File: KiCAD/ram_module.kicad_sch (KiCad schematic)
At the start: 2 parts, among them U30 CY7C199, U31 CY7C199

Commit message: finished schematics and footprint assignments; need to figure out +5v connection issue
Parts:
- U30, U31: footprint (none) -> Package_DIP:DIP-28_W7.62mm
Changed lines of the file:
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@@
 			)
 		)
-		(property "Footprint" ""
+		(property "Footprint" "Package_DIP:DIP-28_W7.62mm"
 			(at 213.36 66.04 0)
 			(effects
@@
 			)
 		)
-		(property "Footprint" ""
+		(property "Footprint" "Package_DIP:DIP-28_W7.62mm"
 			(at 153.67 66.04 0)
 			(effects

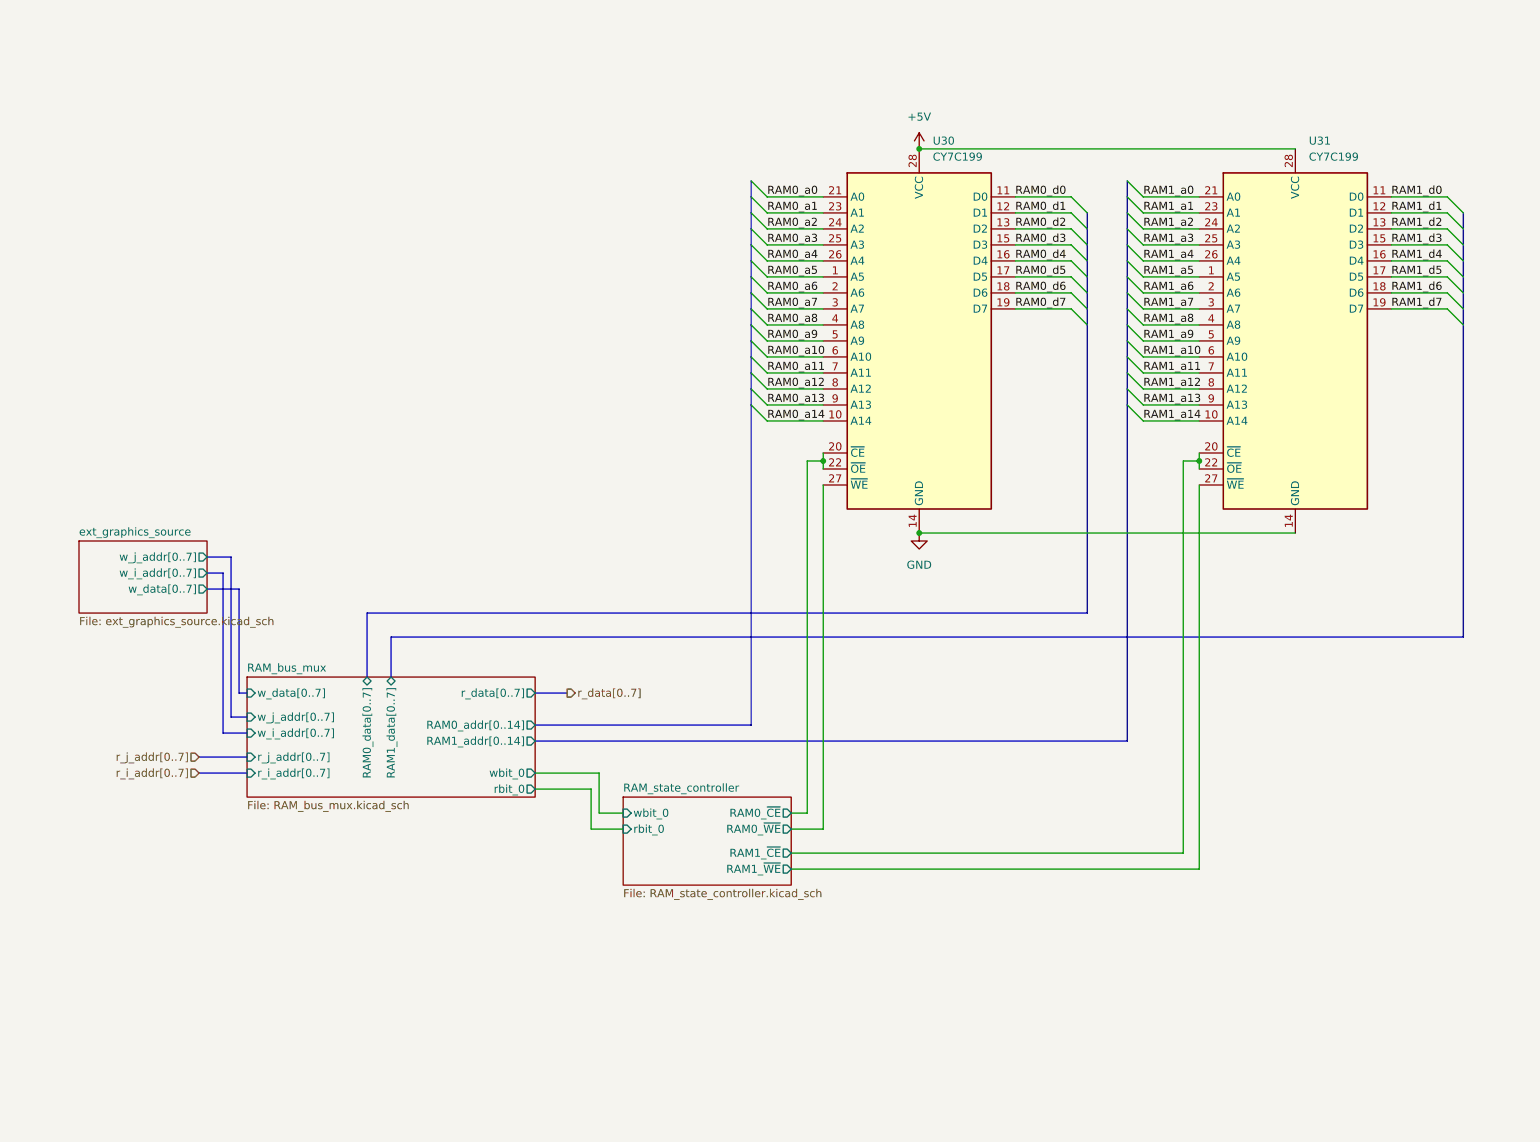
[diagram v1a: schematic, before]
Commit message: modified debug connector; changed board type in pcb editor
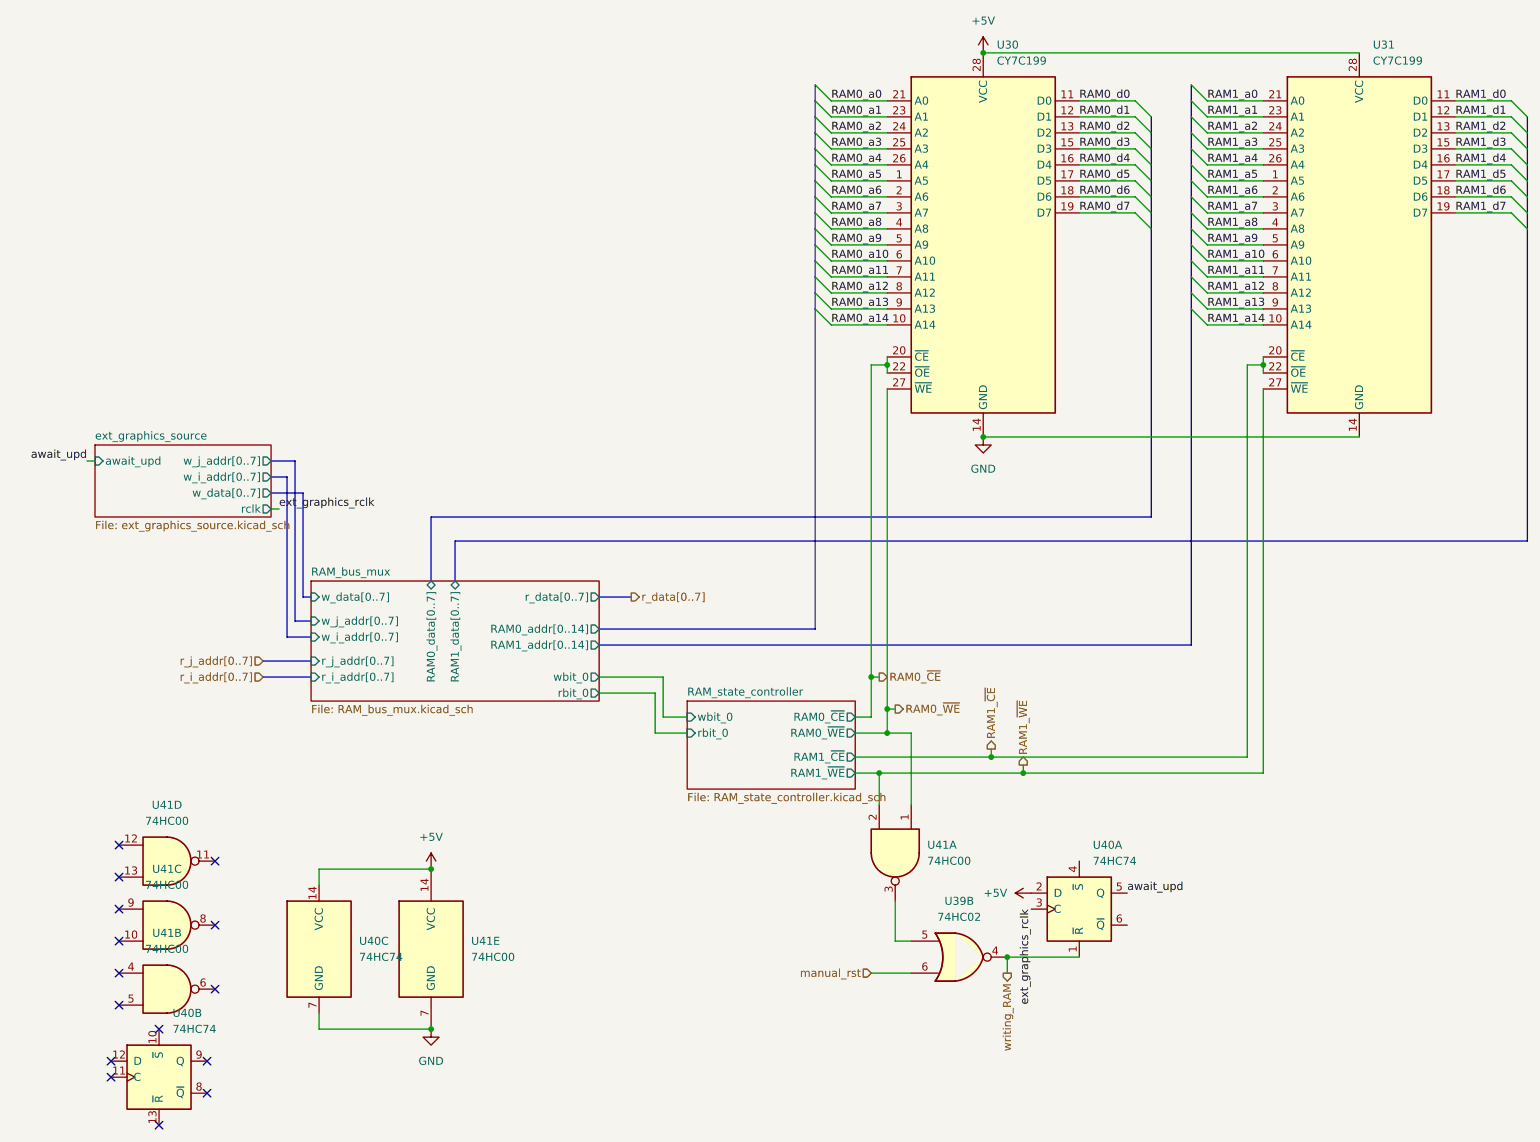
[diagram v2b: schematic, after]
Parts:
- added U39: 74HC02, Package_DIP:DIP-14_W7.62mm, symbol 74xx:74HC02
- added U40: 74HC74, Package_DIP:DIP-14_W7.62mm, symbol 74xx:74HC74
- added U41: 74HC00, Package_DIP:DIP-14_W7.62mm, symbol 74xx:74HC00
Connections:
- net +5V: now also U40.14 (VCC), U40.2 (D), U41.14 (VCC)
- net GND: now also U40.7 (GND), U41.7 (GND)
- net RAM_state_controller/RAM0_~{CE} renamed RAM0_~{CE}
- net RAM_state_controller/RAM0_~{WE} renamed RAM0_~{WE}
- net RAM0_~{WE}: now also U41.1
- net RAM_state_controller/RAM1_~{CE} renamed RAM1_~{CE}
- net RAM_state_controller/RAM1_~{WE} renamed RAM1_~{WE}
- net RAM1_~{WE}: now also U41.2
- new net: U39.5, U41.3
- new net await_upd: U40.5 (Q)
- new net ext_graphics_rclk: U40.3 (C)
- new net manual_rst: U39.6
- new net writing_RAM: U39.4, U40.1 (~{R})
- no-connect marks 0 -> 15
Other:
- sheet ext_graphics_source ports: added await_upd, rclk; removed none
- moved on the sheet: U30, U31

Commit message: fix multiple ERCs that made RAM addrs not connecting
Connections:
- net +5V: now also U40.4 (~{S})
- no-connect marks 15 -> 16
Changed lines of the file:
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@@
 		(at 26.67 171.45)
 	)
+	(no_connect
+		(at 186.69 158.75)
+	)
 	(bus_entry
 		(at 199.39 48.26)
@@
 		)
 	)
-	(wire
-		(pts
-			(xy 199.39 27.94) (xy 208.28 27.94)
-		)
-		(stroke
-			(width 0)
-			(type default)
-		)
-	)
 	(bus
 		(pts
@@
 	(wire
 		(pts
+			(xy 199.39 27.94) (xy 208.28 27.94)
+		)
+		(stroke
+			(width 0)
+			(type default)
+		)
+	)
+	(wire
+		(pts
 			(xy 21.59 85.09) (xy 22.86 85.09)
 		)
@@
 		)
 	)
+	(label "RAM0_d[0..7]"
+		(at 97.79 93.98 0)
+		(effects
+			(font
+				(size 1.27 1.27)
+			)
+			(justify left bottom)
+		)
+	)
 	(label "ext_graphics_rclk"
 		(at 171.45 156.21 270)
@@
 		)
 	)
+	(label "RAM1_d[0..7]"
+		(at 97.79 97.79 0)
+		(effects
+			(font
+				(size 1.27 1.27)
+			)
+			(justify left bottom)
+		)
+	)
 	(label "RAM1_a9"
 		(at 199.39 50.8 0)
@@
 		)
 	)
+	(label "RAM1_a[0..14]"
+		(at 196.85 85.09 90)
+		(effects
+			(font
+				(size 1.27 1.27)
+			)
+			(justify left bottom)
+		)
+	)
 	(label "RAM1_a7"
 		(at 199.39 45.72 0)
@@
 		)
 	)
+	(label "RAM0_a[0..14]"
+		(at 137.16 82.55 90)
+		(effects
+			(font
+				(size 1.27 1.27)
+			)
+			(justify left bottom)
+		)
+	)
 	(label "RAM1_d3"
 		(at 238.76 35.56 0)
@@
 					(unit 1)
 				)
+			)
+		)
+	)
+	(symbol
+		(lib_id "power:+5V")
+		(at 179.07 148.59 0)
+		(unit 1)
+		(exclude_from_sim no)
+		(in_bom yes)
+		(on_board yes)
+		(dnp no)
+		(fields_autoplaced yes)
+		(property "Reference" "#PWR0122"
+			(at 179.07 152.4 0)
+			(effects
+				(font
+					(size 1.27 1.27)
+				)
+				(hide yes)
+			)
+		)
+		(property "Value" "+5V"
+			(at 179.07 143.51 0)
+			(effects
+				(font
+					(size 1.27 1.27)
+				)
+			)
+		)
+		(property "Footprint" ""
+			(at 179.07 148.59 0)
+			(effects
+				(font
+					(size 1.27 1.27)
+				)
+				(hide yes)
+			)
+		)
+		(property "Datasheet" ""
+			(at 179.07 148.59 0)
+			(effects
+				(font
+					(size 1.27 1.27)
+				)
+				(hide yes)
+			)
+		)
+		(property "Description" "Power symbol creates a global label with name \"+5V\""
+			(at 179.07 148.59 0)
+			(effects
+				(font
+					(size 1.27 1.27)
+				)
+				(hide yes)
+			)
+		)
+		(pin "1"
+		)
+		(instances
+			(project ""
+				(path "/53ebbfbe-eaa1-4706-acc1-611a99db7179/a295050b-d209-4efc-8327-c0e97d5127bf"
+					(reference "#PWR0122")
+					(unit 1)
+				)

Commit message: resolve ERCs for addr combiner
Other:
- sheet ext_graphics_source ports: added data[0..7], i_addr[0..7], j_addr[0..7]; removed w_data[0..7], w_i_addr[0..7], w_j_addr[0..7]
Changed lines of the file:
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@@
 			)
 		)
-		(pin "w_i_addr[0..7]" output
+		(pin "i_addr[0..7]" output
 			(at 50.8 87.63 0)
 			(effects
@@
 			)
 		)
-		(pin "w_data[0..7]" output
+		(pin "data[0..7]" output
 			(at 50.8 90.17 0)
 			(effects
@@
 			)
 		)
-		(pin "w_j_addr[0..7]" output
+		(pin "j_addr[0..7]" output
 			(at 50.8 85.09 0)
 			(effects

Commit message: passed DRC for PCB
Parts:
- added J7: Conn_02x08_Odd_Even, Connector_PinSocket_2.54mm:PinSocket_2x08_P2.54mm_Vertical, symbol Connector_Generic:Conn_02x08_Odd_Even
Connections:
- net RAM0_d0: now also J7.1 (Pin_1)
- net RAM0_d1: now also J7.3 (Pin_3)
- net RAM0_d2: now also J7.5 (Pin_5)
- net RAM0_d3: now also J7.7 (Pin_7)
- net RAM0_d4: now also J7.9 (Pin_9)
- net RAM0_d5: now also J7.11 (Pin_11)
- net RAM0_d6: now also J7.13 (Pin_13)
- net RAM0_d7: now also J7.15 (Pin_15)
- net RAM1_d0: now also J7.2 (Pin_2)
- net RAM1_d1: now also J7.4 (Pin_4)
- net RAM1_d2: now also J7.6 (Pin_6)
- net RAM1_d3: now also J7.8 (Pin_8)
- net RAM1_d4: now also J7.10 (Pin_10)
- net RAM1_d5: now also J7.12 (Pin_12)
- net RAM1_d6: now also J7.14 (Pin_14)
- net RAM1_d7: now also J7.16 (Pin_16)
- net can_upd: now reaches U40.6 (~{Q})
- net await_upd: no longer names the net of U40.5 (Q)
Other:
- sheet ext_graphics_source ports: added can_upd; removed await_upd
- note added: "when 0: processing, when 1: availabel to write"
